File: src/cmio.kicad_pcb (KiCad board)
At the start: 2 copper layers, 78.7 x 29.2 mm, 35 parts, among them J1 USB_POWER, J3 BANK0, J4 USB_OTG, J5 CM3Lite, J6 TVOUT, J7 BANK1, J8 Micro_SD_Card_TFP09_2_12B, SW1 Reset, U1 AP3417B, U2 AP3417B, U3 SP6203EM5-L-2-8/TR, U4 AP2401

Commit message: Add GND VIAs
Signed-off-by: Mahyar Koshkouei <mahyar.koshkouei@gmail.com>
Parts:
- moved C4 1.20 mm to (106.7, 96.4), turned to 180 degrees
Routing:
- net GND: track 134.6 -> 203.6 mm, vias 4 -> 10
- net (no net): track 10.5 -> 0.00 mm
- net +3V3: track 114.5 -> 115.3 mm

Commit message: Add test points
Signed-off-by: Mahyar Koshkouei <mahyar.koshkouei@gmail.com>
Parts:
- added 5V: TEST, Measurement_Points:Measurement_Point_Round-SMD-Pad_Small, B.Cu at (134.1, 105.7)
- added GND: TEST, Measurement_Points:Measurement_Point_Round-SMD-Pad_Small, B.Cu at (136.5, 107.2)
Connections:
- J1 pad 2: (no net) -> Net-(J1-Pad2)
- J1 pad 3: (no net) -> Net-(J1-Pad3)
- J1 pad 4: (no net) -> Net-(J1-Pad4)
- J5 pad 100: (no net) -> Net-(J5-Pad100)
- J5 pad 101: (no net) -> Net-(J5-Pad101)
- J5 pad 102: (no net) -> Net-(J5-Pad102)
- J5 pad 105: (no net) -> Net-(J5-Pad105)
- J5 pad 106: (no net) -> Net-(J5-Pad106)
- J5 pad 107: (no net) -> Net-(J5-Pad107)
- J5 pad 108: (no net) -> Net-(J5-Pad108)
- J5 pad 111: (no net) -> Net-(J5-Pad111)
- J5 pad 112: (no net) -> Net-(J5-Pad112)
- J5 pad 113: (no net) -> Net-(J5-Pad113)
- J5 pad 114: (no net) -> Net-(J5-Pad114)
- J5 pad 117: (no net) -> Net-(J5-Pad117)
- J5 pad 118: (no net) -> Net-(J5-Pad118)
- J5 pad 119: (no net) -> Net-(J5-Pad119)
- J5 pad 120: (no net) -> Net-(J5-Pad120)
- J5 pad 123: (no net) -> Net-(J5-Pad123)
- J5 pad 125: (no net) -> Net-(J5-Pad125)
- J5 pad 129: (no net) -> Net-(J5-Pad129)
- J5 pad 131: (no net) -> Net-(J5-Pad131)
- J5 pad 135: (no net) -> Net-(J5-Pad135)
- J5 pad 136: (no net) -> Net-(J5-Pad136)
- J5 pad 137: (no net) -> Net-(J5-Pad137)
- J5 pad 138: (no net) -> Net-(J5-Pad138)
- J5 pad 141: (no net) -> Net-(J5-Pad141)
- J5 pad 142: (no net) -> Net-(J5-Pad142)
- J5 pad 143: (no net) -> Net-(J5-Pad143)
- J5 pad 144: (no net) -> Net-(J5-Pad144)
- J5 pad 147: (no net) -> Net-(J5-Pad147)
- J5 pad 148: (no net) -> Net-(J5-Pad148)
- J5 pad 149: (no net) -> Net-(J5-Pad149)
- J5 pad 150: (no net) -> Net-(J5-Pad150)
- J5 pad 153: (no net) -> Net-(J5-Pad153)
- J5 pad 155: (no net) -> Net-(J5-Pad155)
- J5 pad 159: (no net) -> Net-(J5-Pad159)
- J5 pad 161: (no net) -> Net-(J5-Pad161)
- J5 pad 171: (no net) -> Net-(J5-Pad171)
- J5 pad 172: (no net) -> Net-(J5-Pad172)
- J5 pad 173: (no net) -> Net-(J5-Pad173)
- J5 pad 174: (no net) -> Net-(J5-Pad174)
- J5 pad 175: (no net) -> Net-(J5-Pad175)
- J5 pad 176: (no net) -> Net-(J5-Pad176)
- J5 pad 178: (no net) -> Net-(J5-Pad178)
- J5 pad 179: (no net) -> Net-(J5-Pad179)
- J5 pad 180: (no net) -> Net-(J5-Pad180)
- J5 pad 2: (no net) -> Net-(J5-Pad2)
- J5 pad 88: (no net) -> Net-(J5-Pad88)
- J5 pad 90: (no net) -> Net-(J5-Pad90)
- J5 pad 93: (no net) -> Net-(J5-Pad93)
- J5 pad 94: (no net) -> Net-(J5-Pad94)
- J5 pad 95: (no net) -> Net-(J5-Pad95)
- J5 pad 96: (no net) -> Net-(J5-Pad96)
- J5 pad 99: (no net) -> Net-(J5-Pad99)
- J8 pad 9: (no net) -> Net-(J8-Pad9)
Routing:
- net GND: track 203.6 -> 210.0 mm
- net +5V: track 60.6 -> 64.7 mm, vias 2 -> 3
- net OTGID: track 17.5 -> 18.3 mm
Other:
- board text added: "v0.4"

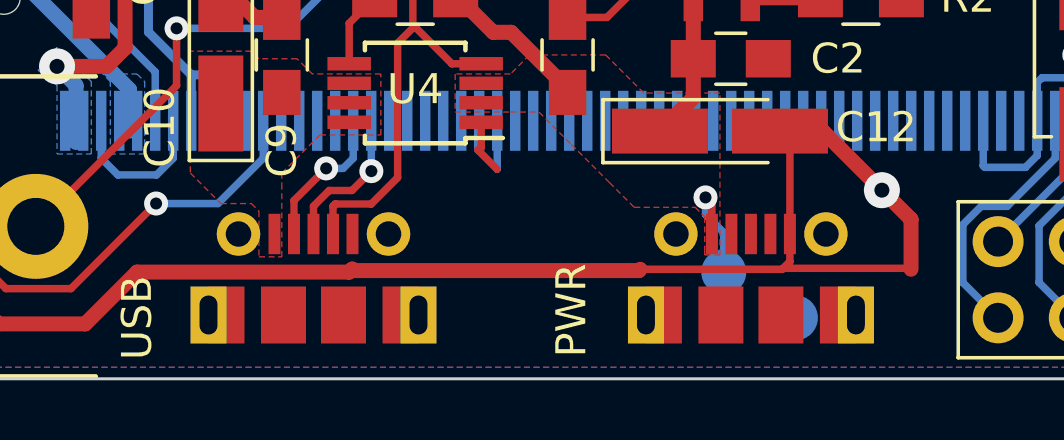
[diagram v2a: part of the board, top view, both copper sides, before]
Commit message: Change Micro USB footprint with circular pads only
For support with OSH Park.

Signed-off-by: Mahyar Koshkouei <mahyar.koshkouei@gmail.com>
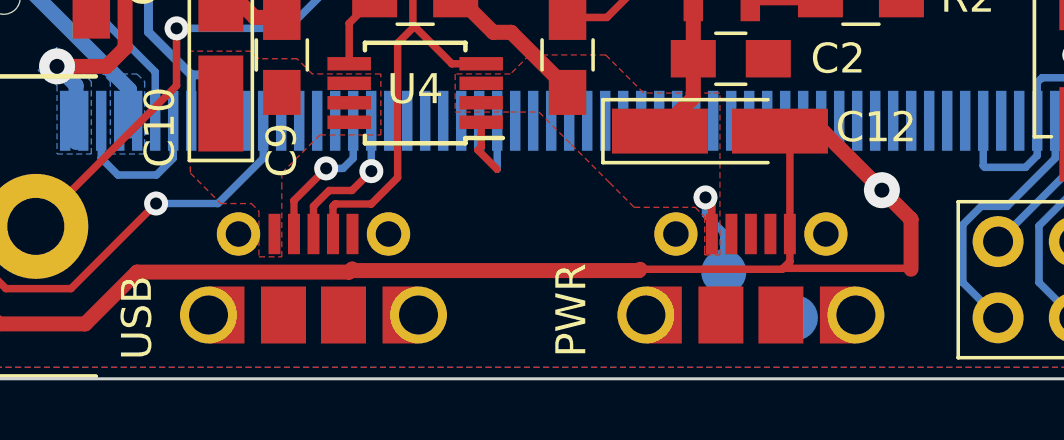
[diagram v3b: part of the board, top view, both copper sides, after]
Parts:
- J1, J4: footprint foot:Molex_Right_Angle_SMT_TypeB_MicroUSB_105017 -> foot:Molex_Right_Angle_SMT_TypeB_MicroUSB_105017_CircularOnly
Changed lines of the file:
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@@
     )
-  )
-  (module foot:Molex_Right_Angle_SMT_TypeB_MicroUSB_105017 (layer F.Cu)
-    (at 120.436 104.394)
-    (fp_text reference J4 (at -4.104 0) (layer F.SilkS) hide
-      (effects (font (size 1 1) (thickness 0.15)))
-    )
-    (fp_text value USB_OTG (at 0 -3) (layer F.Fab)
-      (effects (font (size 1 1) (thickness 0.15)))
-    )
-    (fp_line (start -4.826 4.064) (end -4.826 -1.27) (layer F.CrtYd) (width 0.15))
-    (fp_line (start 4.826 4.064) (end -4.826 4.064) (layer F.CrtYd) (width 0.15))
-    (fp_line (start 4.826 -1.27) (end 4.826 4.064) (layer F.CrtYd) (width 0.15))
-    (fp_line (start -4.826 -1.27) (end 4.826 -1.27) (layer F.CrtYd) (width 0.15))
-    (fp_line (start -5 -1.4) (end -5 4.15) (layer F.Fab) (width 0.15))
-    (fp_line (start 5 -1.4) (end -5 -1.4) (layer F.Fab) (width 0.15))
-    (fp_line (start 5 4.15) (end 5 -1.4) (layer F.Fab) (width 0.15))
-    (fp_line (start -5 4.85) (end 5 4.85) (layer F.Fab) (width 0.15))
-    (fp_line (start -5 4.15) (end 5 4.15) (layer F.Fab) (width 0.15))
-    (pad "" smd rect (at 2.9 2.7) (size 1.2 1.9) (layers F.Cu F.Paste F.Mask))
-    (pad "" smd rect (at -2.9 2.7) (size 1.2 1.9) (layers F.Cu F.Paste F.Mask))
-    (pad "" smd rect (at 1 2.7) (size 1.5 1.9) (layers F.Cu F.Paste F.Mask))
-    (pad "" thru_hole rect (at 3.5 2.7) (size 1.2 1.9) (drill oval 0.6 1.3) (layers *.Cu *.Mask))
-    (pad "" thru_hole rect (at -3.5 2.7) (size 1.2 1.9) (drill oval 0.6 1.3) (layers *.Cu *.Mask))
-    (pad "" smd rect (at -1 2.7) (size 1.5 1.9) (layers F.Cu F.Paste F.Mask))
-    (pad 5 smd rect (at 1.3 0) (size 0.4 1.35) (layers F.Cu F.Paste F.Mask)
-      (net 2 GND))
-    (pad 4 smd rect (at 0.65 0) (size 0.4 1.35) (layers F.Cu F.Paste F.Mask)
-      (net 34 OTGID))
-    (pad 2 smd rect (at -0.65 0) (size 0.4 1.35) (layers F.Cu F.Paste F.Mask)
-      (net 36 /D-))
-    (pad 1 smd rect (at -1.3 0) (size 0.4 1.35) (layers F.Cu F.Paste F.Mask)
-      (net 63 "Net-(C10-Pad1)"))
-    (pad 3 smd rect (at 0 0) (size 0.4 1.35) (layers F.Cu F.Paste F.Mask)
-      (net 35 /D+))
-    (pad "" thru_hole circle (at 2.5 0) (size 1.45 1.45) (drill 0.85) (layers *.Cu *.Mask))
-    (pad "" thru_hole circle (at -2.5 0) (size 1.45 1.45) (drill 0.85) (layers *.Cu *.Mask))
-  )
-  (module foot:Molex_Right_Angle_SMT_TypeB_MicroUSB_105017 (layer F.Cu)
-    (at 135.016 104.394)
-    (fp_text reference J1 (at 0 -2) (layer F.SilkS) hide
-      (effects (font (size 1 1) (thickness 0.15)))
-    )
-    (fp_text value USB_POWER (at 0 -3) (layer F.Fab)
-      (effects (font (size 1 1) (thickness 0.15)))
-    )
-    (fp_line (start -4.826 4.064) (end -4.826 -1.27) (layer F.CrtYd) (width 0.15))
-    (fp_line (start 4.826 4.064) (end -4.826 4.064) (layer F.CrtYd) (width 0.15))
-    (fp_line (start 4.826 -1.27) (end 4.826 4.064) (layer F.CrtYd) (width 0.15))
-    (fp_line (start -4.826 -1.27) (end 4.826 -1.27) (layer F.CrtYd) (width 0.15))
-    (fp_line (start -5 -1.4) (end -5 4.15) (layer F.Fab) (width 0.15))
-    (fp_line (start 5 -1.4) (end -5 -1.4) (layer F.Fab) (width 0.15))
-    (fp_line (start 5 4.15) (end 5 -1.4) (layer F.Fab) (width 0.15))
-    (fp_line (start -5 4.85) (end 5 4.85) (layer F.Fab) (width 0.15))
-    (fp_line (start -5 4.15) (end 5 4.15) (layer F.Fab) (width 0.15))
-    (pad "" smd rect (at 2.9 2.7) (size 1.2 1.9) (layers F.Cu F.Paste F.Mask))
-    (pad "" smd rect (at -2.9 2.7) (size 1.2 1.9) (layers F.Cu F.Paste F.Mask))
-    (pad "" smd rect (at 1 2.7) (size 1.5 1.9) (layers F.Cu F.Paste F.Mask))
-    (pad "" thru_hole rect (at 3.5 2.7) (size 1.2 1.9) (drill oval 0.6 1.3) (layers *.Cu *.Mask))
-    (pad "" thru_hole rect (at -3.5 2.7) (size 1.2 1.9) (drill oval 0.6 1.3) (layers *.Cu *.Mask))
-    (pad "" smd rect (at -1 2.7) (size 1.5 1.9) (layers F.Cu F.Paste F.Mask))
-    (pad 5 smd rect (at 1.3 0) (size 0.4 1.35) (layers F.Cu F.Paste F.Mask)
-      (net 2 GND))
-    (pad 4 smd rect (at 0.65 0) (size 0.4 1.35) (layers F.Cu F.Paste F.Mask)
-      (net 71 "Net-(J1-Pad4)"))
-    (pad 2 smd rect (at -0.65 0) (size 0.4 1.35) (layers F.Cu F.Paste F.Mask)
-      (net 72 "Net-(J1-Pad2)"))
-    (pad 1 smd rect (at -1.3 0) (size 0.4 1.35) (layers F.Cu F.Paste F.Mask)
-      (net 1 +5V))
-    (pad 3 smd rect (at 0 0) (size 0.4 1.35) (layers F.Cu F.Paste F.Mask)
-      (net 73 "Net-(J1-Pad3)"))
-    (pad "" thru_hole circle (at 2.5 0) (size 1.45 1.45) (drill 0.85) (layers *.Cu *.Mask))
-    (pad "" thru_hole circle (at -2.5 0) (size 1.45 1.45) (drill 0.85) (layers *.Cu *.Mask))
   )
   (module foot:RCA_PHONO (layer F.Cu)
@@
       (net 1 +5V))
   )
+  (module foot:Molex_Right_Angle_SMT_TypeB_MicroUSB_105017_CircularOnly (layer F.Cu)
+    (at 120.436 104.394)
+    (fp_text reference J4 (at -4.104 0) (layer F.SilkS) hide
+      (effects (font (size 1 1) (thickness 0.15)))
+    )
+    (fp_text value USB_OTG (at 0 -3) (layer F.Fab)
+      (effects (font (size 1 1) (thickness 0.15)))
+    )
+    (fp_line (start -4.826 4.064) (end -4.826 -1.27) (layer F.CrtYd) (width 0.15))
+    (fp_line (start 4.826 4.064) (end -4.826 4.064) (layer F.CrtYd) (width 0.15))
+    (fp_line (start 4.826 -1.27) (end 4.826 4.064) (layer F.CrtYd) (width 0.15))
+    (fp_line (start -4.826 -1.27) (end 4.826 -1.27) (layer F.CrtYd) (width 0.15))
+    (fp_line (start -5 -1.4) (end -5 4.15) (layer F.Fab) (width 0.15))
+    (fp_line (start 5 -1.4) (end -5 -1.4) (layer F.Fab) (width 0.15))
+    (fp_line (start 5 4.15) (end 5 -1.4) (layer F.Fab) (width 0.15))
+    (fp_line (start -5 4.85) (end 5 4.85) (layer F.Fab) (width 0.15))
+    (fp_line (start -5 4.15) (end 5 4.15) (layer F.Fab) (width 0.15))
+    (pad "" smd rect (at 2.9 2.7) (size 1.2 1.9) (layers F.Cu F.Paste F.Mask))
+    (pad "" smd rect (at -2.9 2.7) (size 1.2 1.9) (layers F.Cu F.Paste F.Mask))
+    (pad "" smd rect (at 1 2.7) (size 1.5 1.9) (layers F.Cu F.Paste F.Mask))
+    (pad "" thru_hole circle (at 3.5 2.7) (size 1.9 1.9) (drill 1.3) (layers *.Cu *.Mask))
+    (pad "" thru_hole circle (at -3.5 2.7) (size 1.9 1.9) (drill 1.3) (layers *.Cu *.Mask))
+    (pad "" smd rect (at -1 2.7) (size 1.5 1.9) (layers F.Cu F.Paste F.Mask))
+    (pad 5 smd rect (at 1.3 0) (size 0.4 1.35) (layers F.Cu F.Paste F.Mask)
+      (net 2 GND))
+    (pad 4 smd rect (at 0.65 0) (size 0.4 1.35) (layers F.Cu F.Paste F.Mask)
+      (net 34 OTGID))
+    (pad 2 smd rect (at -0.65 0) (size 0.4 1.35) (layers F.Cu F.Paste F.Mask)
+      (net 36 /D-))
+    (pad 1 smd rect (at -1.3 0) (size 0.4 1.35) (layers F.Cu F.Paste F.Mask)
+      (net 63 "Net-(C10-Pad1)"))
+    (pad 3 smd rect (at 0 0) (size 0.4 1.35) (layers F.Cu F.Paste F.Mask)
+      (net 35 /D+))
+    (pad "" thru_hole circle (at 2.5 0) (size 1.45 1.45) (drill 0.85) (layers *.Cu *.Mask))
+    (pad "" thru_hole circle (at -2.5 0) (size 1.45 1.45) (drill 0.85) (layers *.Cu *.Mask))
+  )
+  (module foot:Molex_Right_Angle_SMT_TypeB_MicroUSB_105017_CircularOnly (layer F.Cu)
+    (at 135.016 104.394)
+    (fp_text reference J1 (at -4.104 0) (layer F.SilkS) hide
+      (effects (font (size 1 1) (thickness 0.15)))
+    )
+    (fp_text value USB_POWER (at 0 -3) (layer F.Fab)
+      (effects (font (size 1 1) (thickness 0.15)))
+    )
+    (fp_line (start -4.826 4.064) (end -4.826 -1.27) (layer F.CrtYd) (width 0.15))
+    (fp_line (start 4.826 4.064) (end -4.826 4.064) (layer F.CrtYd) (width 0.15))
+    (fp_line (start 4.826 -1.27) (end 4.826 4.064) (layer F.CrtYd) (width 0.15))
+    (fp_line (start -4.826 -1.27) (end 4.826 -1.27) (layer F.CrtYd) (width 0.15))
+    (fp_line (start -5 -1.4) (end -5 4.15) (layer F.Fab) (width 0.15))
+    (fp_line (start 5 -1.4) (end -5 -1.4) (layer F.Fab) (width 0.15))
+    (fp_line (start 5 4.15) (end 5 -1.4) (layer F.Fab) (width 0.15))
+    (fp_line (start -5 4.85) (end 5 4.85) (layer F.Fab) (width 0.15))
+    (fp_line (start -5 4.15) (end 5 4.15) (layer F.Fab) (width 0.15))
+    (pad "" smd rect (at 2.9 2.7) (size 1.2 1.9) (layers F.Cu F.Paste F.Mask))
+    (pad "" smd rect (at -2.9 2.7) (size 1.2 1.9) (layers F.Cu F.Paste F.Mask))
+    (pad "" smd rect (at 1 2.7) (size 1.5 1.9) (layers F.Cu F.Paste F.Mask))
+    (pad "" thru_hole circle (at 3.5 2.7) (size 1.9 1.9) (drill 1.3) (layers *.Cu *.Mask))
+    (pad "" thru_hole circle (at -3.5 2.7) (size 1.9 1.9) (drill 1.3) (layers *.Cu *.Mask))
+    (pad "" smd rect (at -1 2.7) (size 1.5 1.9) (layers F.Cu F.Paste F.Mask))
+    (pad 5 smd rect (at 1.3 0) (size 0.4 1.35) (layers F.Cu F.Paste F.Mask)
+      (net 2 GND))
+    (pad 4 smd rect (at 0.65 0) (size 0.4 1.35) (layers F.Cu F.Paste F.Mask)
+      (net 71 "Net-(J1-Pad4)"))
+    (pad 2 smd rect (at -0.65 0) (size 0.4 1.35) (layers F.Cu F.Paste F.Mask)
+      (net 72 "Net-(J1-Pad2)"))
+    (pad 1 smd rect (at -1.3 0) (size 0.4 1.35) (layers F.Cu F.Paste F.Mask)
+      (net 1 +5V))
+    (pad 3 smd rect (at 0 0) (size 0.4 1.35) (layers F.Cu F.Paste F.Mask)
+      (net 73 "Net-(J1-Pad3)"))
+    (pad "" thru_hole circle (at 2.5 0) (size 1.45 1.45) (drill 0.85) (layers *.Cu *.Mask))
+    (pad "" thru_hole circle (at -2.5 0) (size 1.45 1.45) (drill 0.85) (layers *.Cu *.Mask))
+  )
   (gr_text v0.4 (at 181.61 99.06 90) (layer F.SilkS)

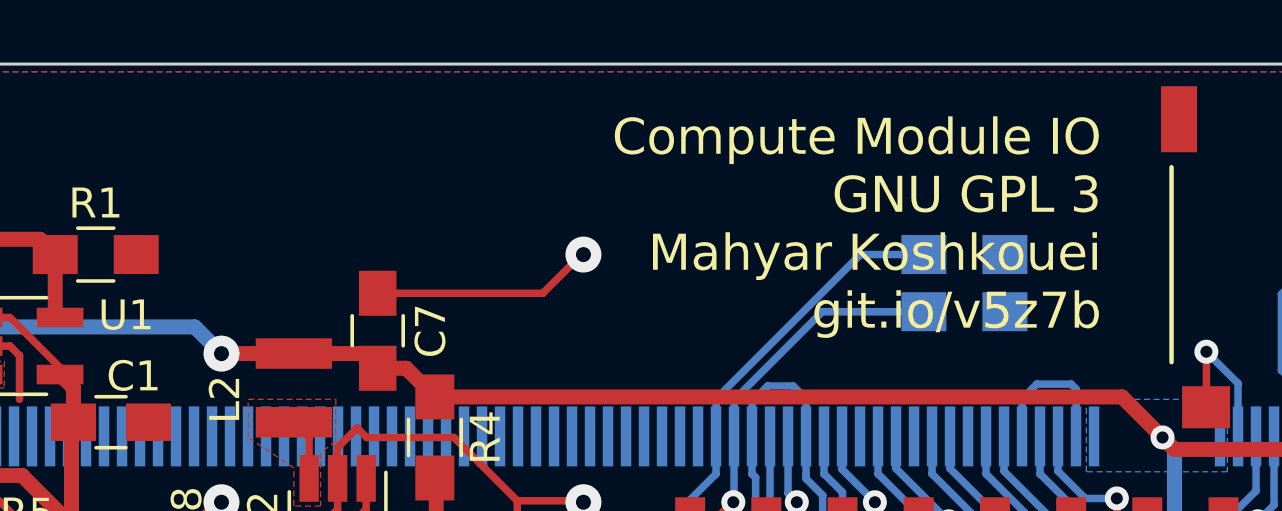
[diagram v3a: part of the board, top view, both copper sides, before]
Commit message: Change license to TAPR Open Hardware License
Signed-off-by: Mahyar Koshkouei <mahyar.koshkouei@gmail.com>
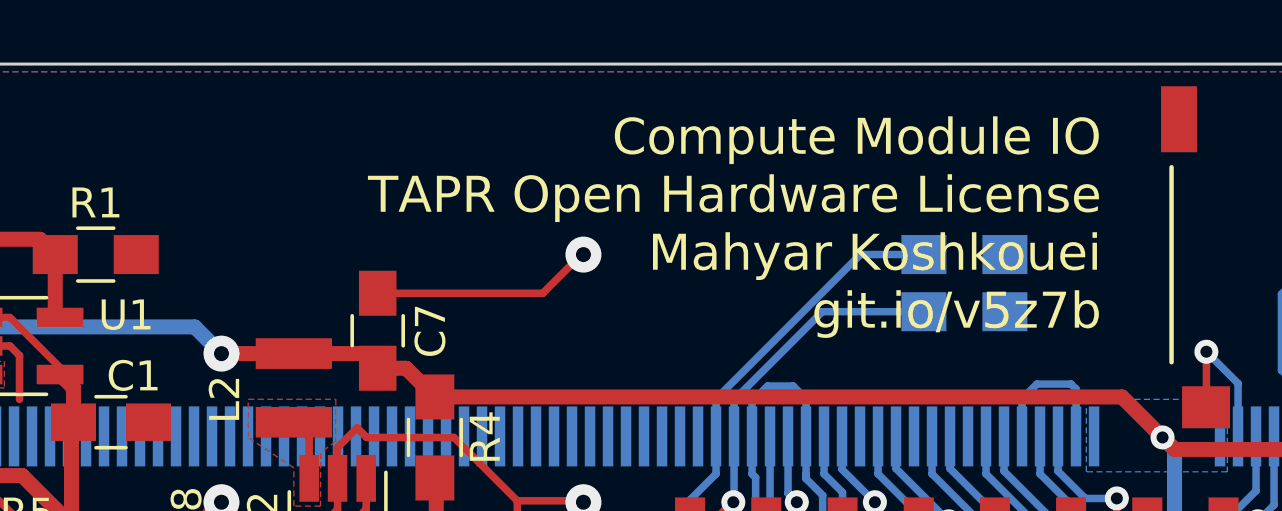
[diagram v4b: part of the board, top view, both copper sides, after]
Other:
- board text added: "Compute Module IO TAPR Open Hardware License Mahyar Koshkouei git.io/v5z7b"
- board text removed: "Compute Module IO GNU GPL 3 Mahyar Koshkouei git.io/v5z7b"
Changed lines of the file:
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@@
     (links 224)
     (no_connects 10)
-    (area 104.089999 79.959999 182.930001 109.270001)
+    (area 90.702001 54.244999 193.785001 122.080001)
     (thickness 1.6)
     (drawings 17)
@@
     (effects (font (size 1 1) (thickness 0.15)))
   )
-  (gr_text "Compute Module IO\nGNU GPL 3\nMahyar Koshkouei\ngit.io/v5z7b" (at 159.512 85.344) (layer F.SilkS)
+  (gr_text "Compute Module IO\nTAPR Open Hardware License\nMahyar Koshkouei\ngit.io/v5z7b" (at 159.512 85.344) (layer F.SilkS)
     (effects (font (size 1.2 1.2) (thickness 0.25)) (justify right))
   )
